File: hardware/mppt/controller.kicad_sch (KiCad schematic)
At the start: 39 parts, among them SW201 SW_SPST, U201 STM32F446RETx, Y201 16MHz, Y202 32kHz

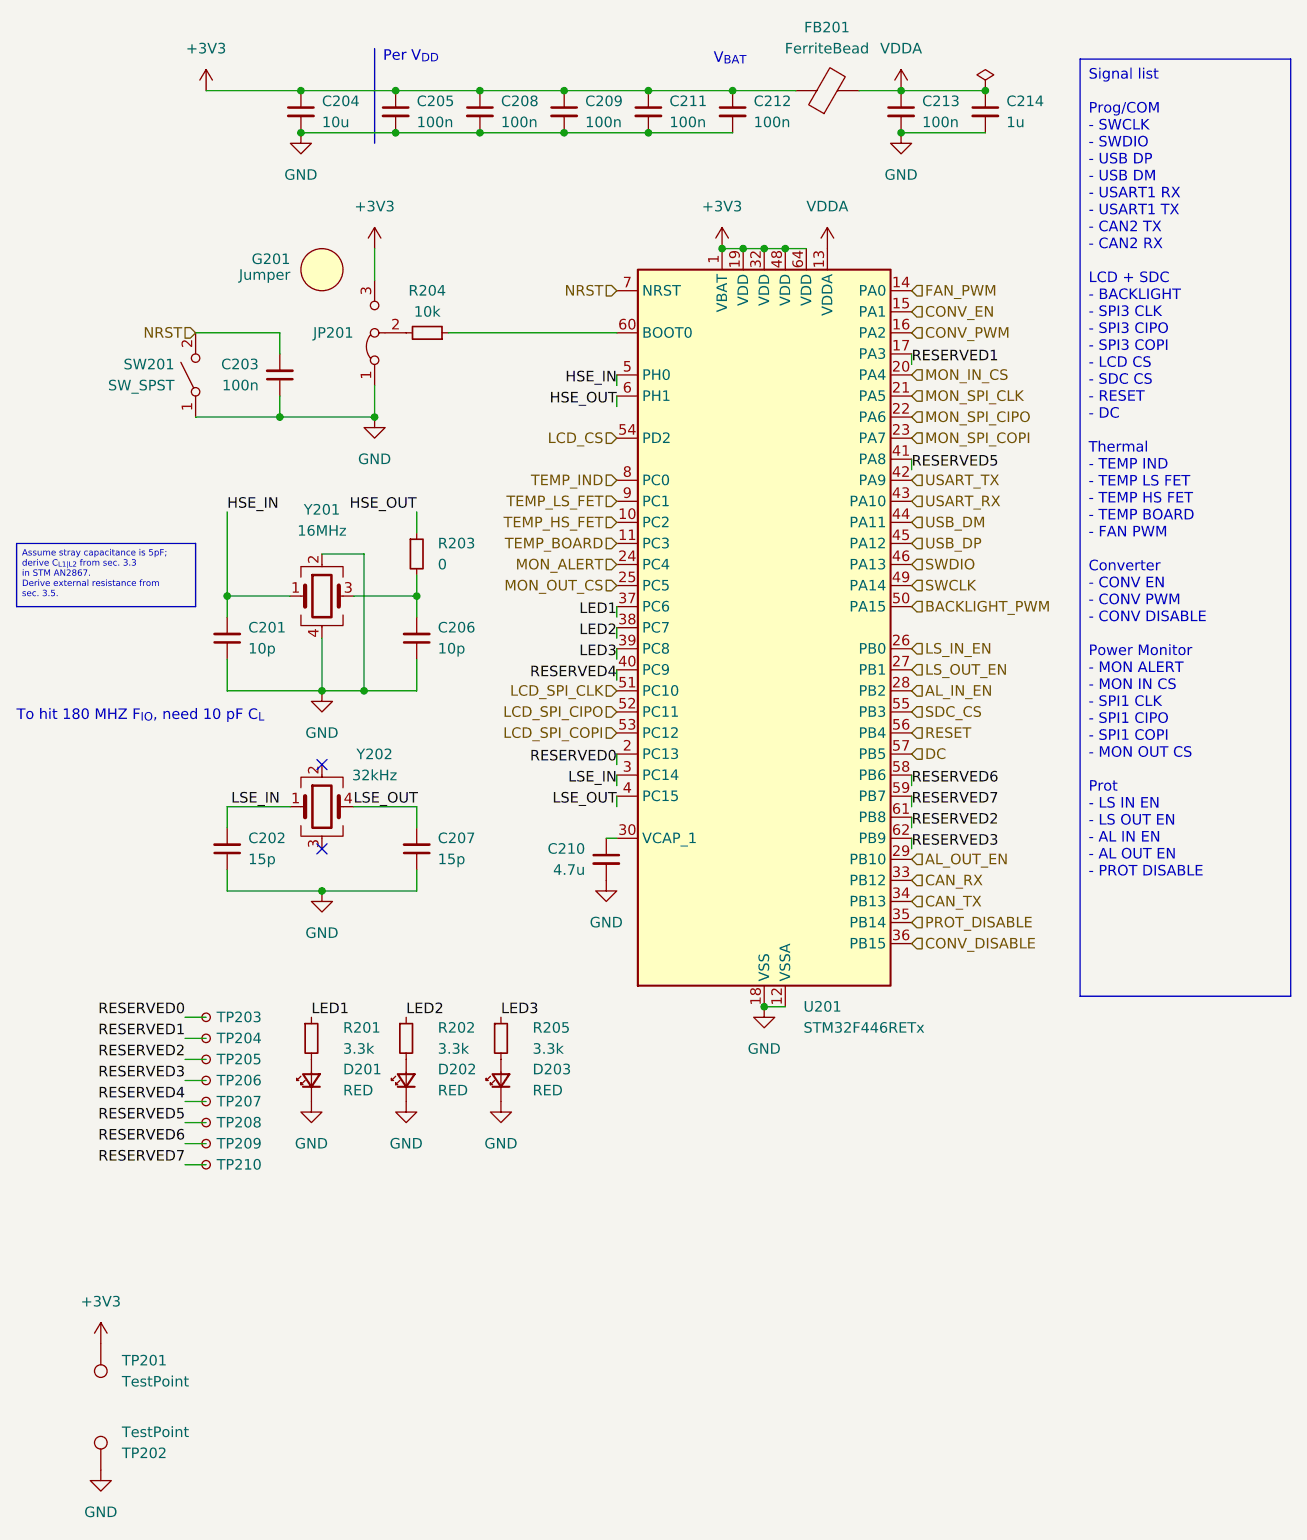
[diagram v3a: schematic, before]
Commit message: PCB variant for power regulation breakout.
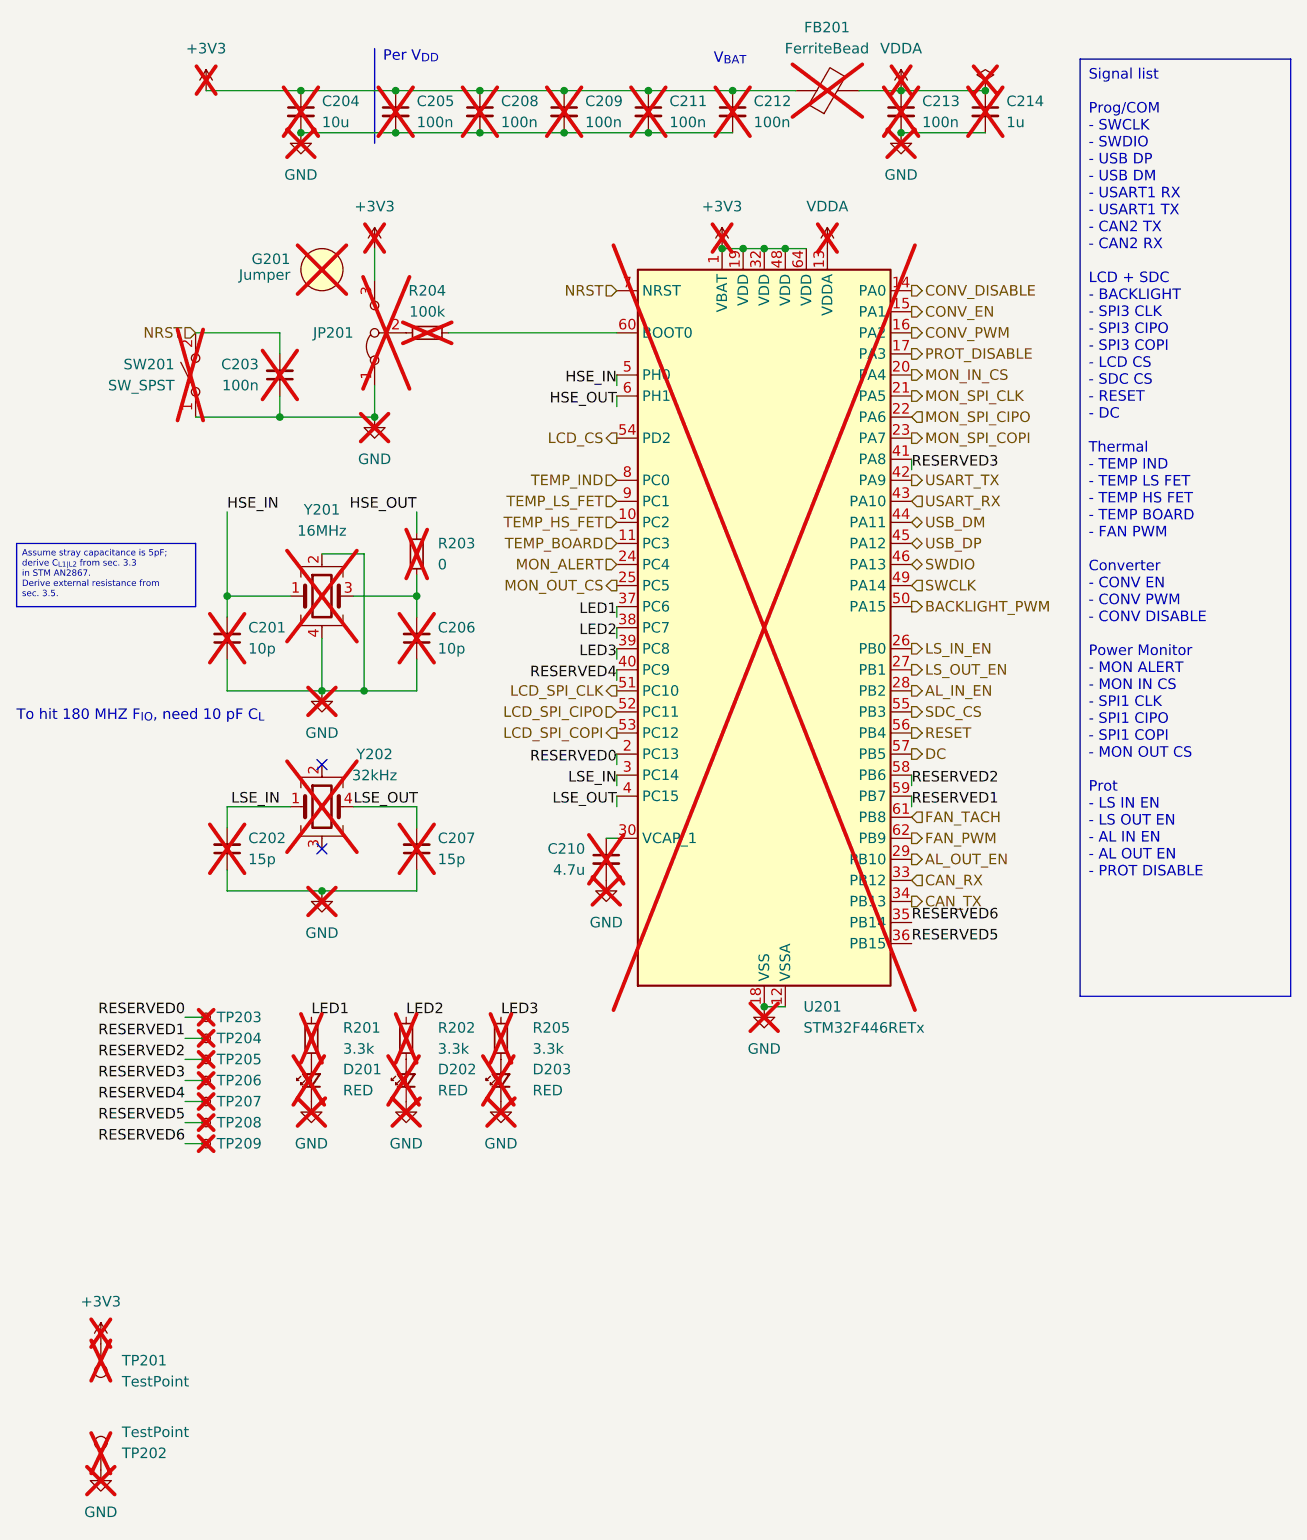
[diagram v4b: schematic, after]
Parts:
- removed TP210: TestPoint_Small, TestPoint:TestPoint_Pad_D1.0mm, symbol Connector:TestPoint_Small
- C201, C202, C203, C204, C205, C206, C207, C208, C209, C210, C211, C212, C213, C214, D201, D202, D203, FB201, G201, R201, R202, R203, R205, SW201, TP201, TP202, TP203, TP204, TP205, TP206, TP207, TP208, TP209, U201, Y201, Y202: now not fitted; now left out of the parts list
- JP201: now not fitted
- R204: value 10k -> 100k; P/N CRCW060310K0FKEA -> CRCW0603100KFKEA; now not fitted; now left out of the parts list
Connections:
- net RESERVED7 is gone; now on net RESERVED1: U201.59 (PB7)
- net CONV_DISABLE: now also U201.14 (PA0); no longer U201.36 (PB15)
- net FAN_PWM: now also U201.62 (PB9); no longer U201.14 (PA0)
- net PROT_DISABLE: now also U201.17 (PA3); no longer U201.35 (PB14)
- net RESERVED1: no longer U201.17 (PA3)
- net RESERVED2: now also U201.58 (PB6); no longer U201.61 (PB8)
- net RESERVED3: now also U201.41 (PA8); no longer U201.62 (PB9)
- net RESERVED5: now also U201.36 (PB15); no longer U201.41 (PA8)
- net RESERVED6: now also U201.35 (PB14); no longer U201.58 (PB6)
- new net FAN_TACH: U201.61 (PB8)

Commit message: complete layout, drc, signaling optimizations and added dnp testpoints
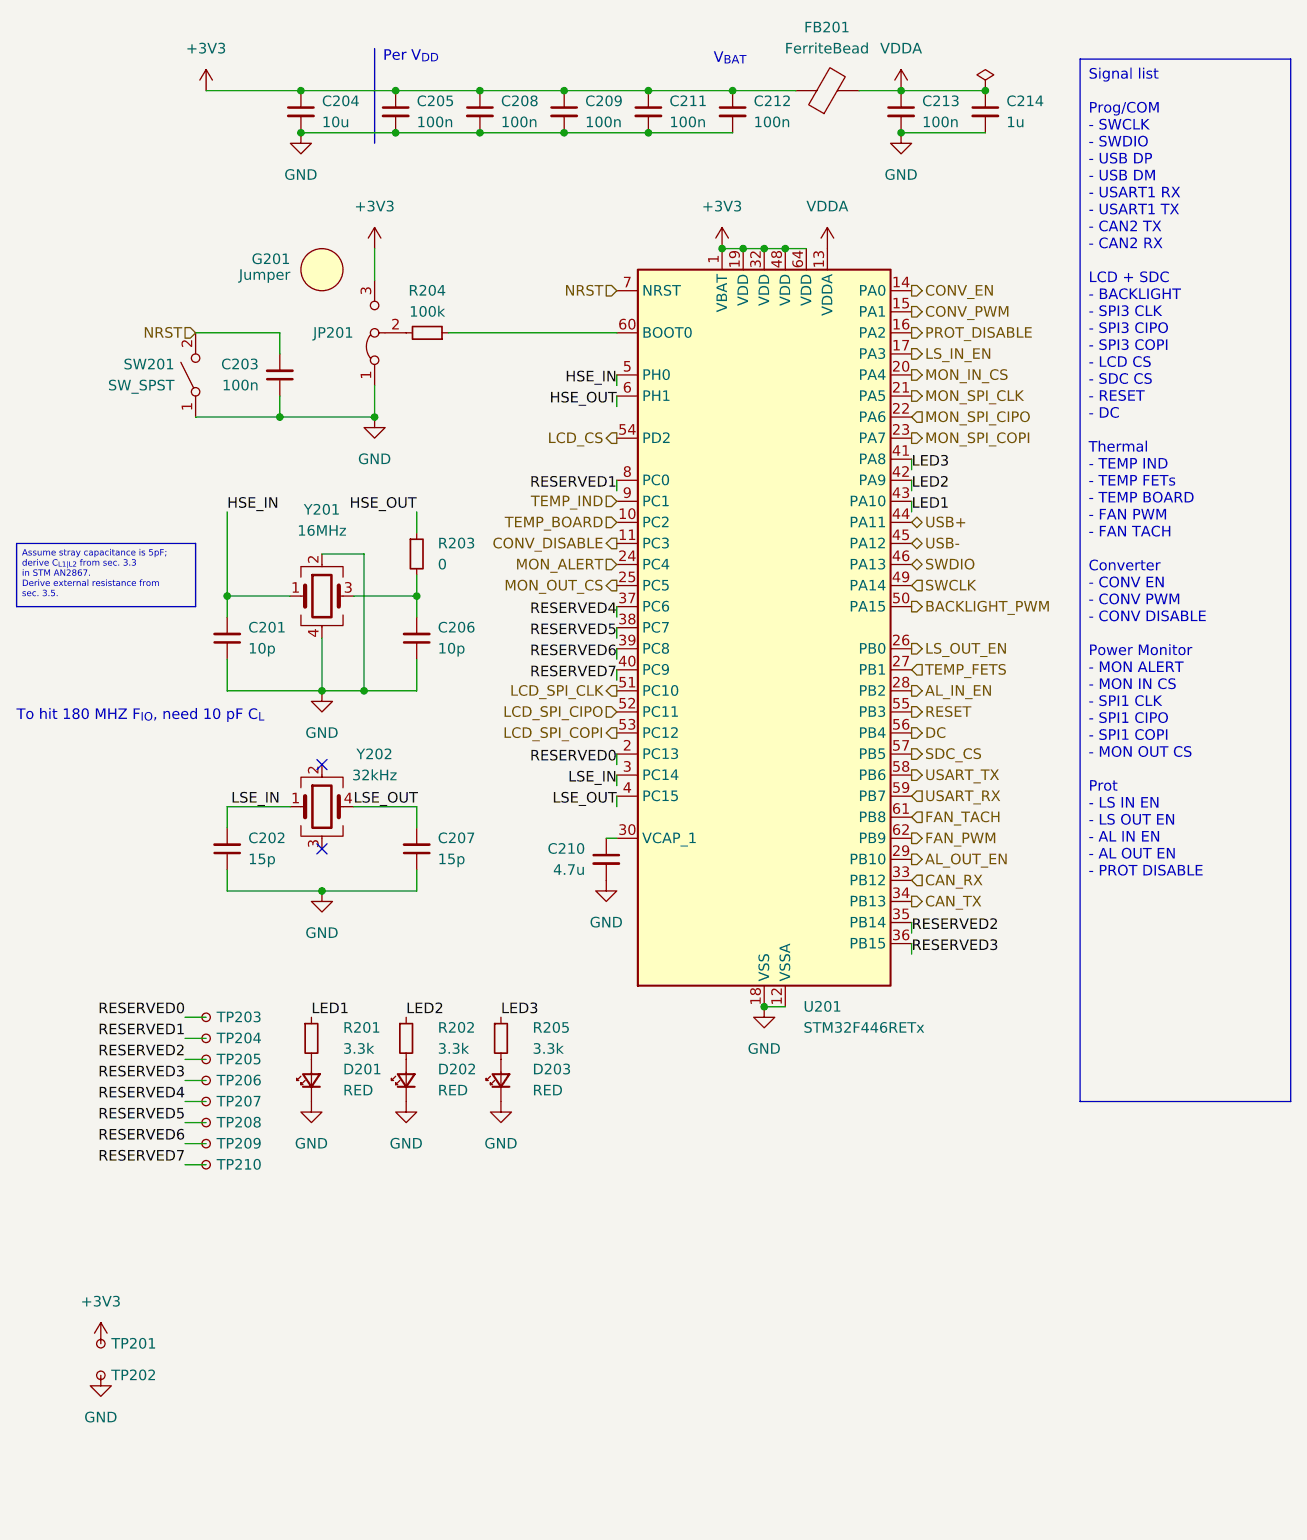
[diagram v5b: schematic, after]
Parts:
- removed TP201, TP202: TestPoint, TestPoint:TestPoint_Keystone_5000-5004_Miniature, symbol Connector:TestPoint
- added TP201, TP202, TP210: TestPoint_Small, TestPoint:TestPoint_Pad_D1.0mm, symbol Connector:TestPoint_Small
- C201, C202, C203, C204, C205, C206, C207, C208, C209, C210, C211, C212, C213, C214, D201, D202, D203, FB201, G201, JP201, R201, R202, R203, R204, R205, SW201, TP203, TP204, TP205, TP206, TP207, TP208, TP209, U201, Y201, Y202: now fitted; now in the parts list
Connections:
- net TEMP_HS_FET is gone; now on net TEMP_BOARD: U201.10 (PC2)
- net TEMP_LS_FET is gone; now on net TEMP_IND: U201.9 (PC1)
- net +3V3: now also TP201.1
- net CONV_DISABLE: now also U201.11 (PC3); no longer U201.14 (PA0)
- net CONV_EN: now also U201.14 (PA0); no longer U201.15 (PA1)
- net CONV_PWM: now also U201.15 (PA1); no longer U201.16 (PA2)
- net DC: now also U201.56 (PB4); no longer U201.57 (PB5)
- net GND: now also TP202.1
- net LED1: now also U201.43 (PA10); no longer U201.37 (PC6)
- net LED2: now also U201.42 (PA9); no longer U201.38 (PC7)
- net LED3: now also U201.41 (PA8); no longer U201.39 (PC8)
- net LS_IN_EN: now also U201.17 (PA3); no longer U201.26 (PB0)
- net LS_OUT_EN: now also U201.26 (PB0); no longer U201.27 (PB1)
- net PROT_DISABLE: now also U201.16 (PA2); no longer U201.17 (PA3)
- net RESERVED1: now also U201.8 (PC0); no longer U201.59 (PB7)
- net RESERVED2: now also U201.35 (PB14); no longer U201.58 (PB6)
- net RESERVED3: now also U201.36 (PB15); no longer U201.41 (PA8)
- net RESERVED4: now also U201.37 (PC6); no longer U201.40 (PC9)
- net RESERVED5: now also U201.38 (PC7); no longer U201.36 (PB15)
- net RESERVED6: now also U201.39 (PC8); no longer U201.35 (PB14)
- net RESET: now also U201.55 (PB3); no longer U201.56 (PB4)
- net SDC_CS: now also U201.57 (PB5); no longer U201.55 (PB3)
- net TEMP_BOARD: no longer U201.11 (PC3)
- net TEMP_IND: no longer U201.8 (PC0)
- net USART_RX: now also U201.59 (PB7); no longer U201.43 (PA10)
- net USART_TX: now also U201.58 (PB6); no longer U201.42 (PA9)
- net USB_DM renamed USB+
- net USB_DP renamed USB-
- new net RESERVED7: TP210.1, U201.40 (PC9)
- new net TEMP_FETS: U201.27 (PB1)

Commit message: converter schematic and layout.
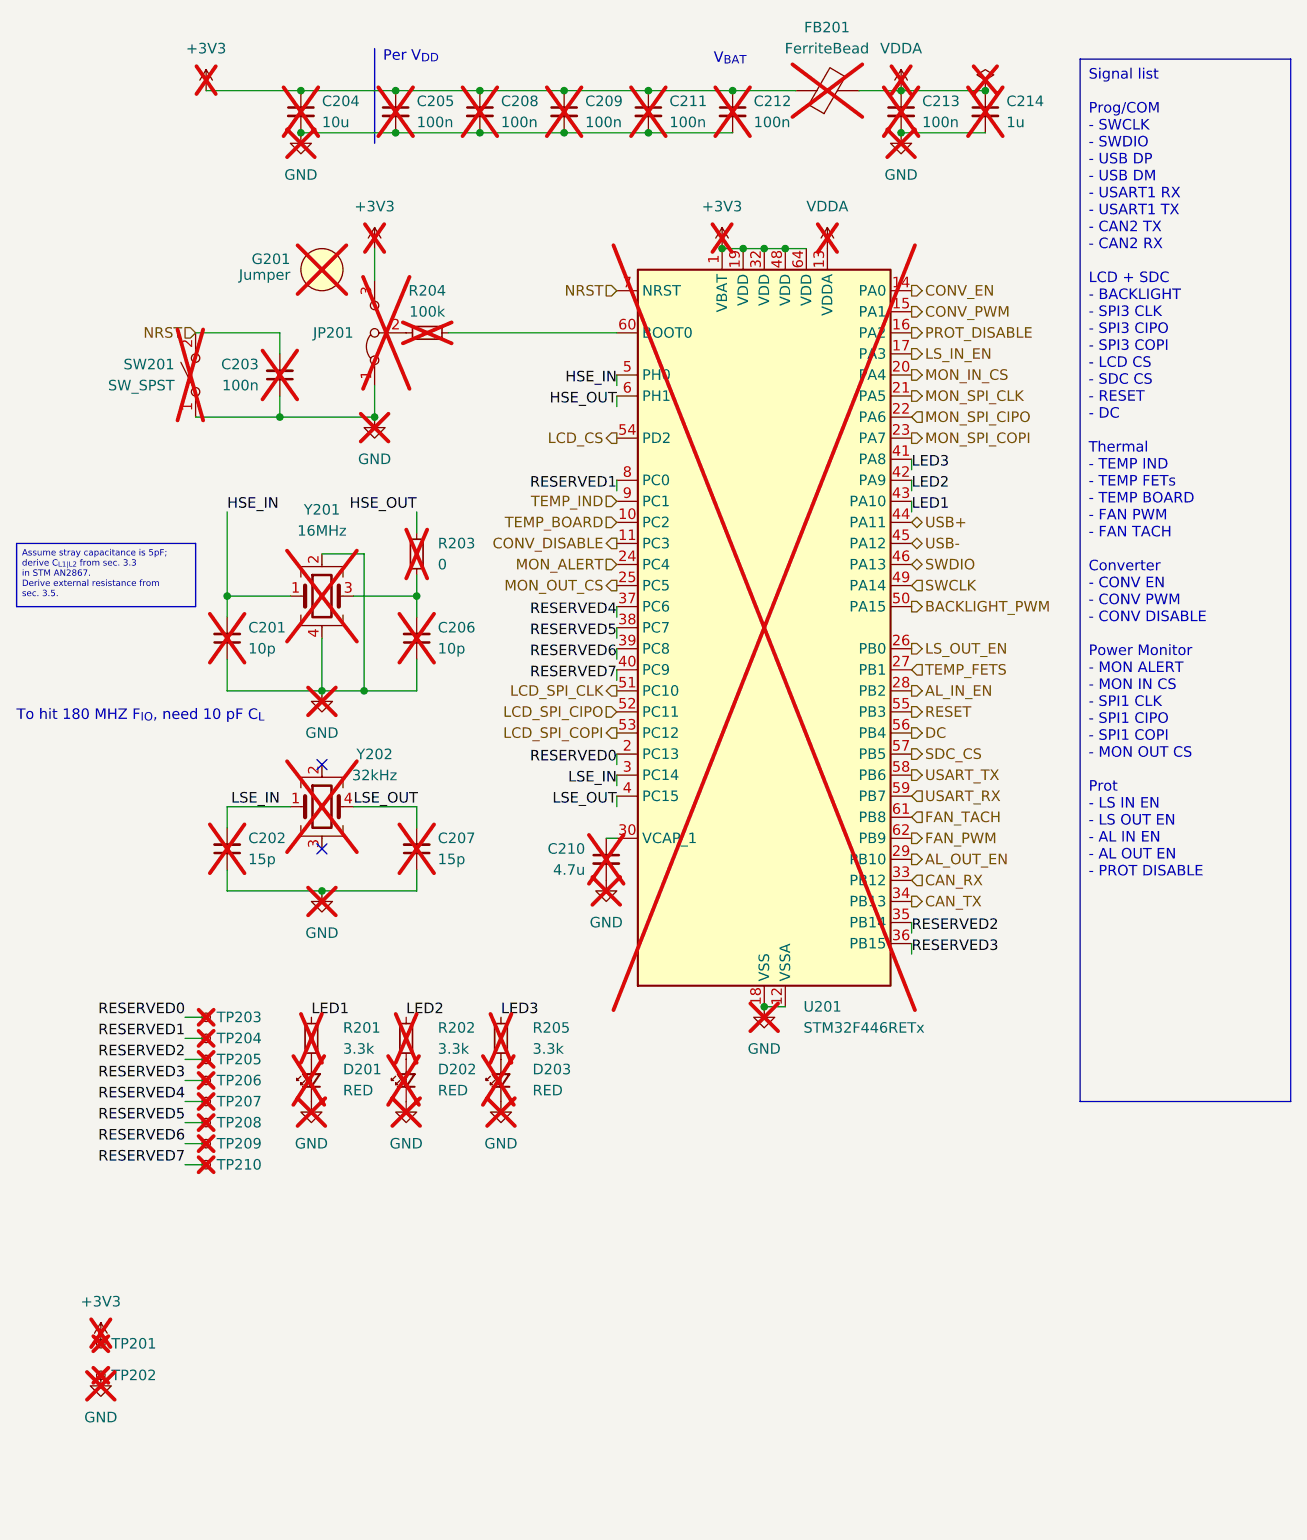
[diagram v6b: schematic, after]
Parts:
- C201, C202, C203, C204, C205, C206, C207, C208, C209, C210, C211, C212, C213, C214, D201, D202, D203, FB201, G201, JP201, R201, R202, R204, R205, SW201, TP201, TP202, TP203, TP204, TP205, TP206, TP207, TP208, TP209, TP210, U201, Y201, Y202: now not fitted; now left out of the parts list
- R203: footprint Resistor_SMD:R_1210_3225Metric_Pad1.30x2.65mm_HandSolder -> Resistor_SMD:R_0805_2012Metric_Pad1.20x1.40mm_HandSolder; P/N CRCW12100000Z0EA -> CRCW08050000Z0EAHP; now not fitted; now left out of the parts list
